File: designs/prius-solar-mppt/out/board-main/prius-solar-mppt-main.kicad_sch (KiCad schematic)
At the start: 0 parts

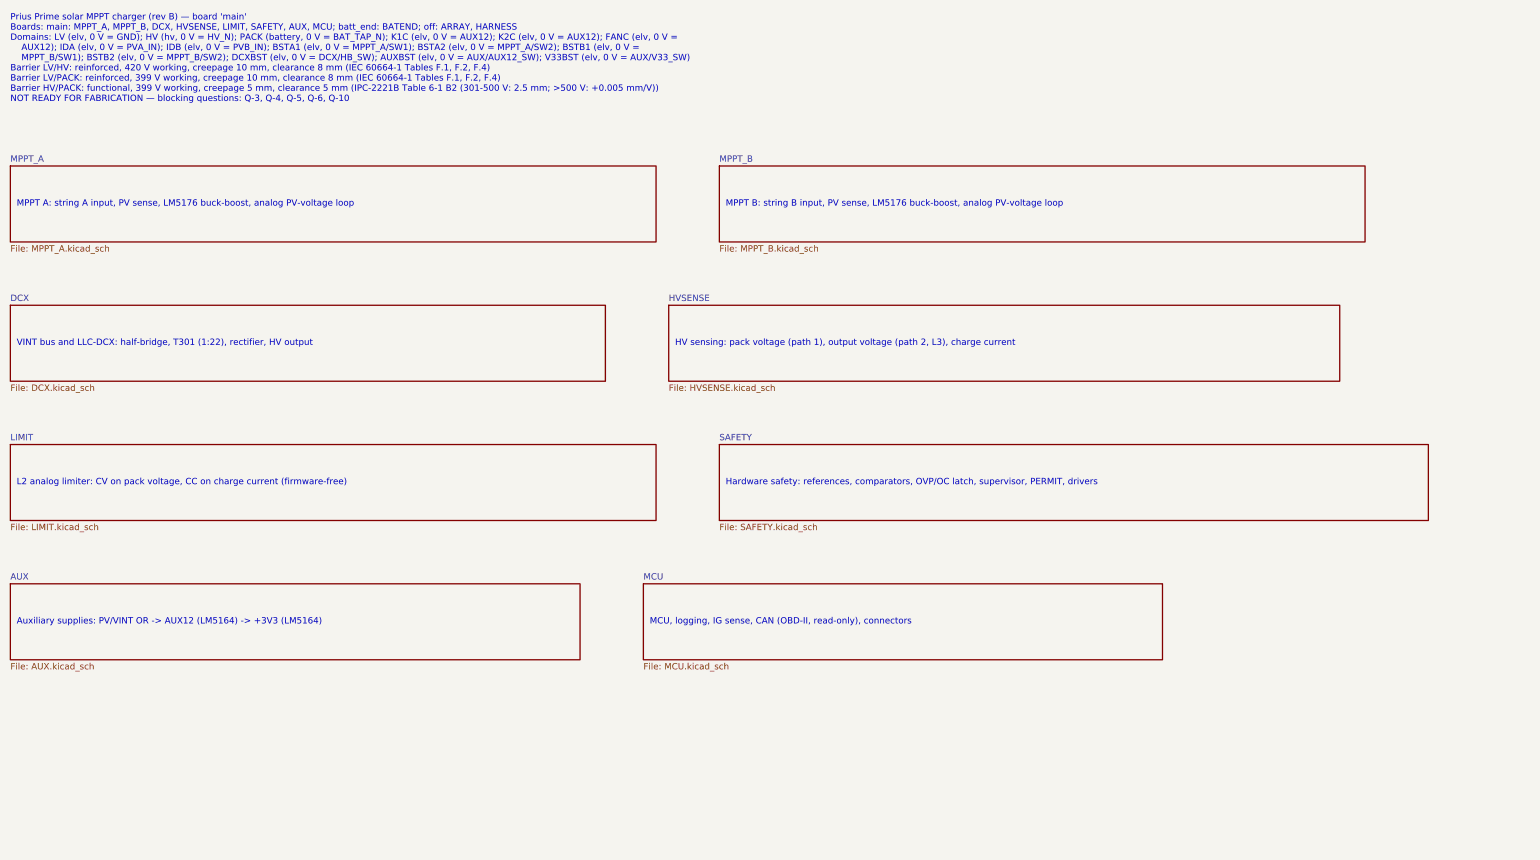
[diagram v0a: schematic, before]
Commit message: designs/prius-solar-mppt: v0.3, fix the independent review's blockers and majors
- B1: CHASSIS domain with reinforced DC barriers to HV and PACK (10/8 mm), HV/PACK edge
  clearance 10 mm, mounting holes fixed with 13 mm keep-outs; thermal pedestal under LV
  parts only.
- B2: no primary source for the Prime's full-charge cell voltage was found (blocking
  Q-13); hardware clamp set below a 4.00 V/cell floor (L3 3.927 V, worst 3.963 V; L2
  3.836 V; L1 3.79 V) with DNP trim to raise later; until then charging may stop near
  55-65 % SOC.
- Majors: sink clamp + burst disable + PV-node trip and TVS against LM5176 reverse power;
  20 MHz AEC-Q200 crystal for CAN (listen-only start); parked insulation monitoring via a
  110 M bridge (also detects a welded relay); open-sensor-safe hardware OT; CAGE CLAMP HV
  terminals with a lid-switch HVIL; DCX on-time and 17.6 A primary overcurrent latches;
  supercap-held latch that clears overnight.
- Build: 0 errors, ERC clean, system and both board netlists identical; 9 waivers (17
  findings, was 32).

Co-Authored-By: Claude Opus 5.5 <noreply@anthropic.com>
Claude-Session: https://claude.ai/code/session_01VFJn9VbX8h27kf4LpLwEtn
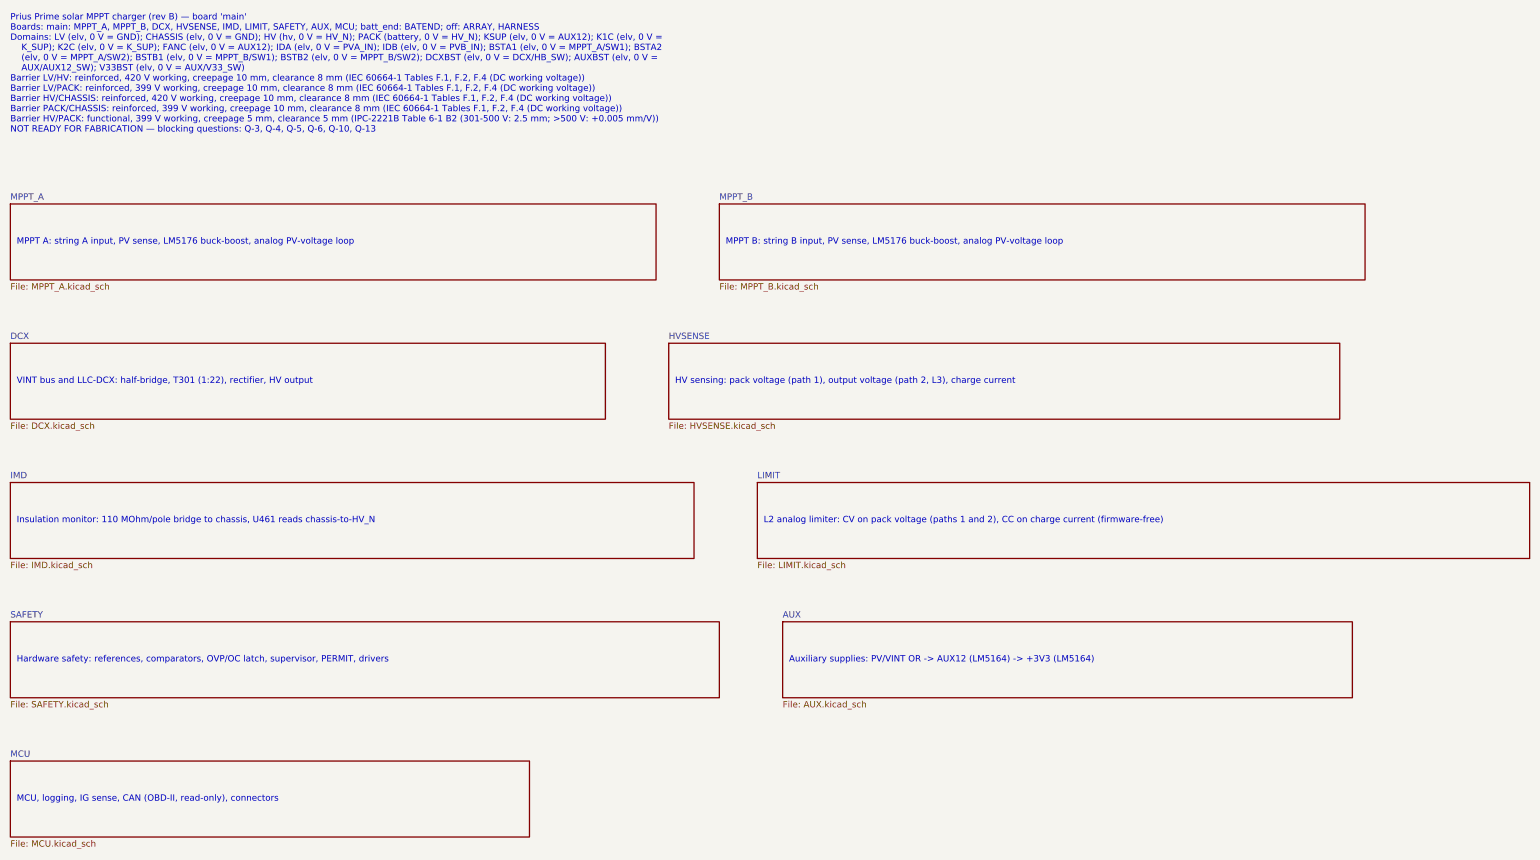
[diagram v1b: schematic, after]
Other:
- added sheet IMD (IMD.kicad_sch)
- note added: "Insulation monitor: 110 MOhm/pole bridge to chassis, U461 reads chassis-to-HV_N"
- note added: "L2 analog limiter: CV on pack voltage (paths 1 and 2), CC on charge current (firmware-free)"
- note added: "Prius Prime solar MPPT charger (rev B) — board 'main' Boards: main: MPPT_A, MPPT_B, DCX, HVSENSE, IMD, LIMIT, SAFETY, AUX, MCU; batt_end: BATEND; off: ARRAY, HARNESS Domains: LV (elv, 0 V = GND); CHASSIS (elv, 0 V = GND); HV (hv, 0 V = HV_N); PACK (battery, 0 V = HV_N); KSUP (elv, 0 V = AUX12); K1C (elv, 0 V = K_SUP); K2C (elv, 0 V = K_SUP); FANC (elv, 0 V = AUX12); IDA (elv, 0 V = PVA_IN); IDB (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"
- note removed: "L2 analog limiter: CV on pack voltage, CC on charge current (firmware-free)"
- note removed: "Prius Prime solar MPPT charger (rev B) — board 'main' Boards: main: MPPT_A, MPPT_B, DCX, HVSENSE, LIMIT, SAFETY, AUX, MCU; batt_end: BATEND; off: ARRAY, HARNESS Domains: LV (elv, 0 V = GND); HV (hv, 0 V = HV_N); PACK (battery, 0 V = BAT_TAP_N); K1C (elv, 0 V = AUX12); K2C (elv, 0 V = AUX12); FANC (elv, 0 V = AUX12); IDA (elv, 0 V = PVA_IN); IDB (elv, 0 V = PVB_IN); BSTA1 (elv, 0 V = MPPT_A/SW1); 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"
